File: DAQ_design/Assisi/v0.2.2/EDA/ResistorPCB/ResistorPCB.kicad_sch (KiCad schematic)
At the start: 3 parts, among them J1 7-POS Plug Terminal, J2 Two-Probe Measurement

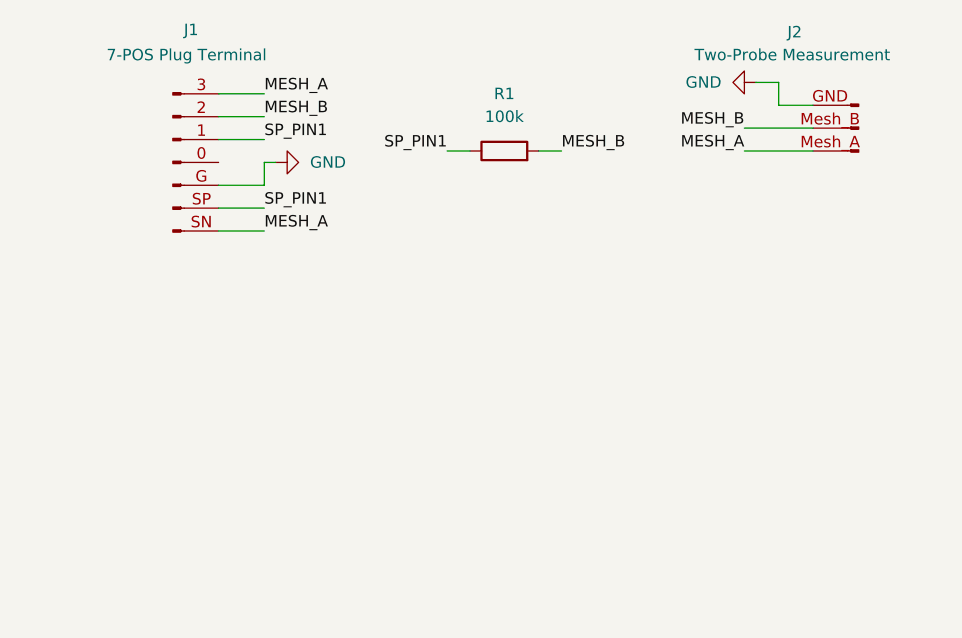
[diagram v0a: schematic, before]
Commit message: Two and Four Probe adapter PCBs
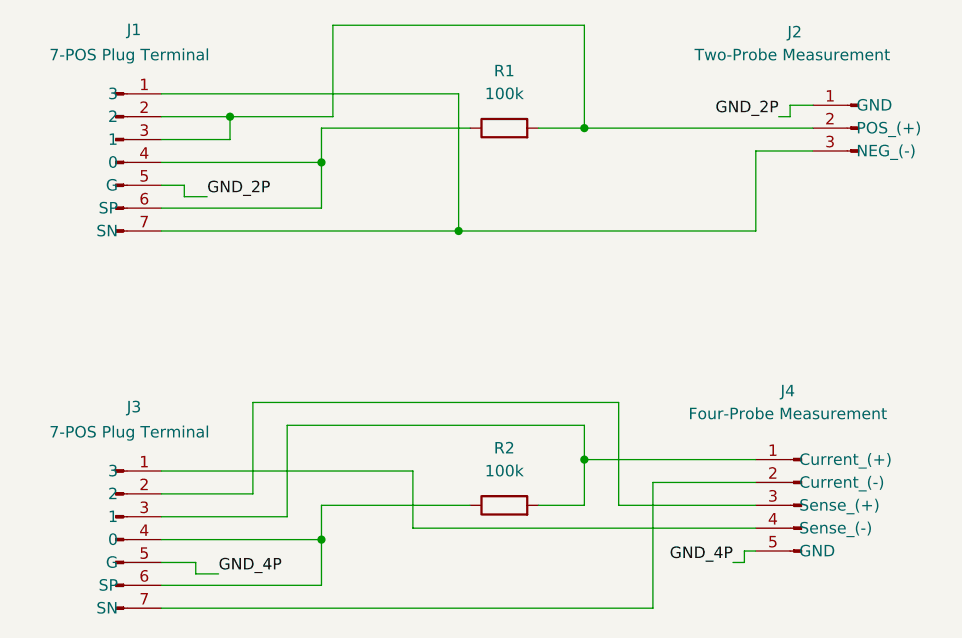
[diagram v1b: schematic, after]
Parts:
- added J3: 7-POS Plug Terminal, EDA Footprint:PHOENIX_1786459, symbol Connector:Conn_01x07_Pin
- added J4: Four-Probe Measurement, Connector_Phoenix_MSTB:PhoenixContact_MSTBA_2,5_5-G-5,08_1x05_P5.08mm_Horizontal, symbol Connector:Conn_01x05_Pin
- added R2: 100k, Resistor_THT:R_Axial_DIN0207_L6.3mm_D2.5mm_P10.16mm_Horizontal, symbol Device:R
- J1: footprint (none) -> EDA Footprint:PHOENIX_1786459
- J2: footprint (none) -> Connector_Phoenix_MSTB:PhoenixContact_MSTBA_2,5_3-G-5,08_1x03_P5.08mm_Horizontal
- R1: footprint (none) -> Resistor_THT:R_Axial_DIN0207_L6.3mm_D2.5mm_P10.16mm_Horizontal
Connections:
- removed net GND: J1.G (Pin_5), J2.GND (Pin_1)
- removed net MESH_A: J1.3 (Pin_1), J1.SN (Pin_7), J2.Mesh_A (Pin_3)
- net MESH_B: no longer names the net of J1.2, R1.2
- net MESH_B: now also J1.3 (1), J2.2 (POS_(+)); no longer J2.Mesh_B (Pin_2)
- removed net SP_PIN1: J1.1 (Pin_3), J1.SP (Pin_6), R1.1
- new net: J3.4 (0), J3.6 (SP), R2.1
- new net: J3.3 (1), J4.1 (Current_(+)), R2.2
- new net: J1.4 (0), J1.6 (SP), R1.1
- new net: J1.1 (3), J1.7 (SN), J2.3 (NEG_(-))
- new net: J3.1 (3), J4.4 (Sense_(-))
- new net: J3.2, J4.3 (Sense_(+))
- new net: J3.7 (SN), J4.2 (Current_(-))
- new net GND_2P: J1.5 (G), J2.1 (GND)
- new net GND_4P: J3.5 (G), J4.5 (GND)
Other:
- moved on the sheet: R1

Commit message: Updates: GND moved, one mounting hole, resistor label moved
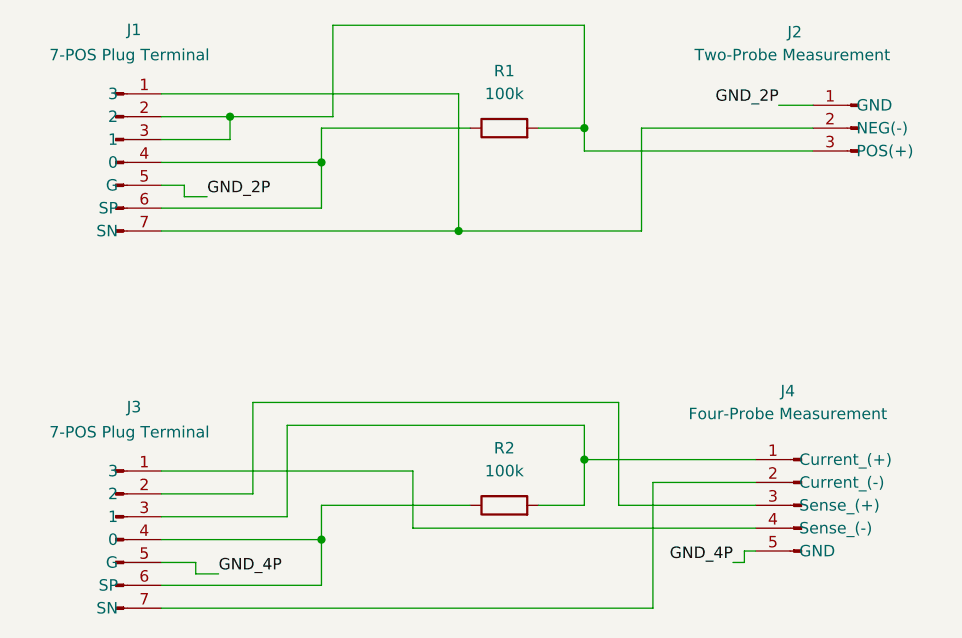
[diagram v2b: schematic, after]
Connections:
- net at J1.2, J1.3 (1), R1.2: now also J2.3 (POS(+)); no longer J2.2 (POS_(+))
- net at J1.1 (3), J1.7 (SN): now also J2.2 (NEG(-)); no longer J2.3 (NEG_(-))
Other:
- moved on the sheet: J2
